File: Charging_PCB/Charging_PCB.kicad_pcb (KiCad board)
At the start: 2 copper layers, 89 x 59.5 mm, 15 parts, among them K3 BMS_Relay, K4 IMD_Relay, Q1 PMOS, Q2 PMOS, U112 Charger Input, U113 Signal Inputs, U114 Relay Output

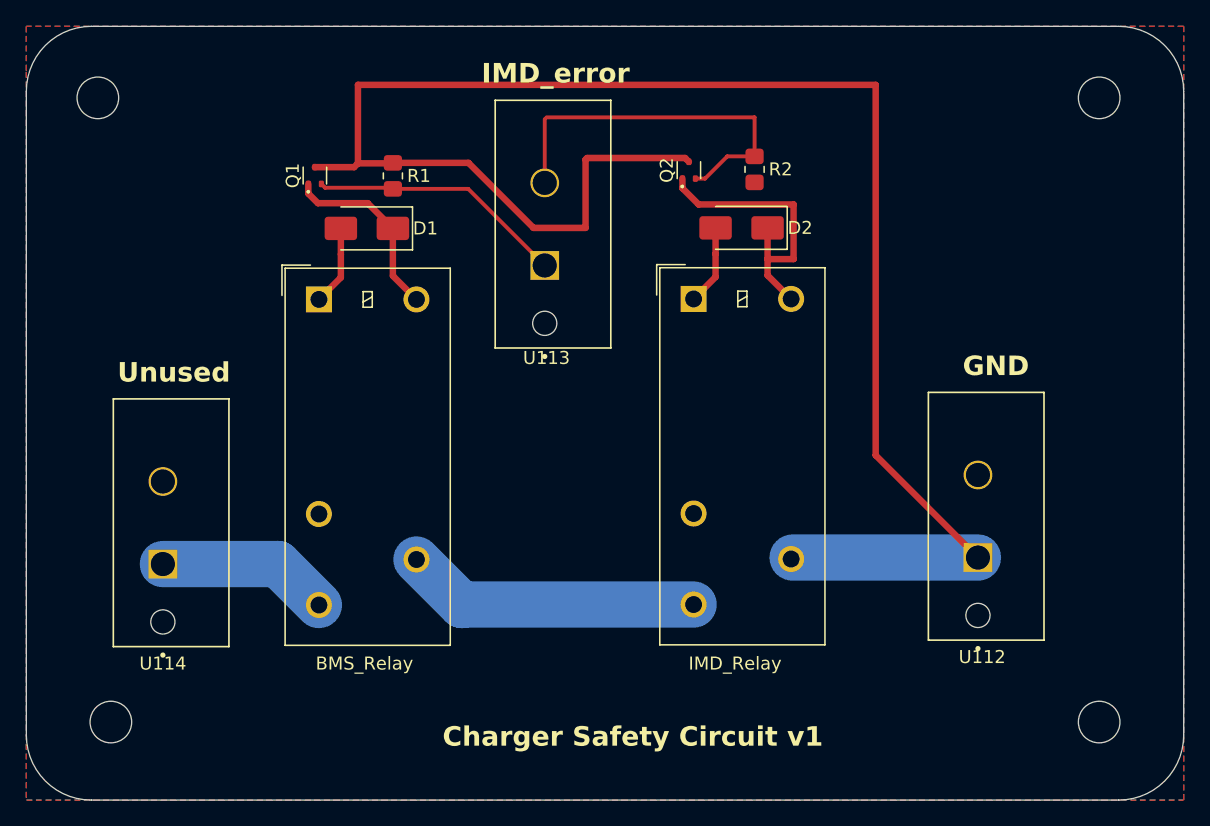
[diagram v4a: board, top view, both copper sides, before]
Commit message: Compacted PCB, and finished BOM,CPL,Gerbers(Charging)
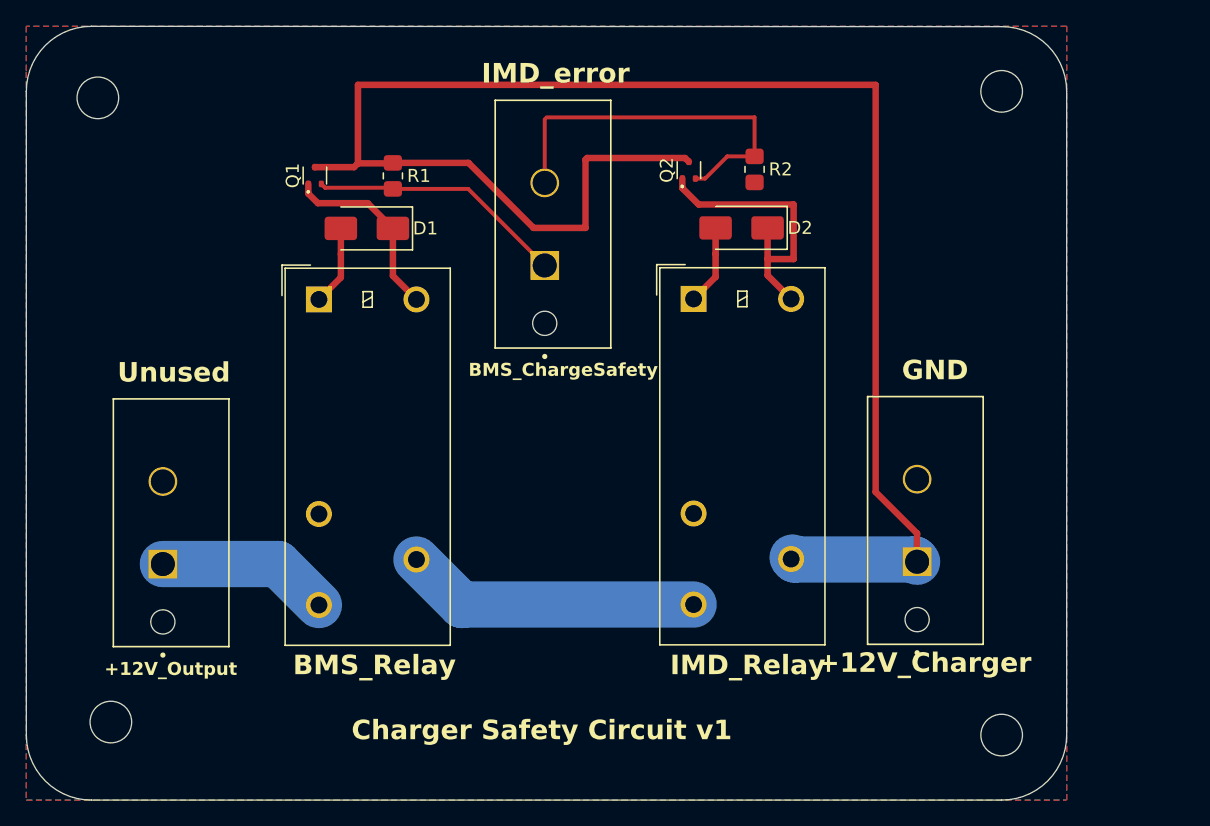
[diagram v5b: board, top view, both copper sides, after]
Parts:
- K3: value BMS_Relay -> Relay_SPDT_Omron_G2RL-1
- K4: value IMD_Relay -> Relay_SPDT_Omron_G2RL-1
- U112: value Charger Input -> 641964-1
- U113: value Signal Inputs -> 641964-1
- U114: value Relay Output -> 641964-1
- moved H103 7.57 mm to (181.5, 128.5)
- moved H101 7.52 mm to (181.5, 79.0)
- moved U112 4.69 mm to (175.0, 115.2)
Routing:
- net +12V: track 136.3 -> 130.1 mm
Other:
- board size 89 x 59.5 mm -> 80 x 59.5 mm
- board text added: "+12V_Charger"
- board text added: "+12V_Output"
- board text added: "BMS_ChargeSafety"
- board text added: "BMS_Relay"
- board text added: "IMD_Relay"

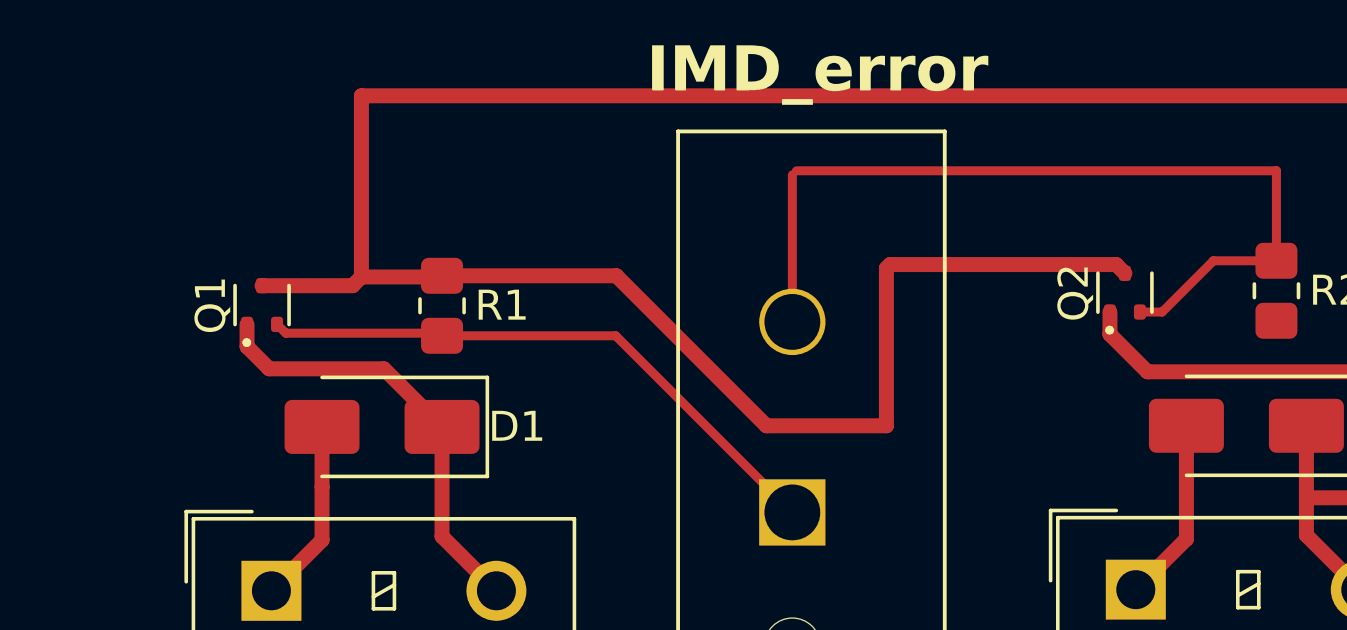
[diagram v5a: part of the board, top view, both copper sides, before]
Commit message: Fixed bad PMOS footprint and symbol, fixed gerbers/BOM/CPL
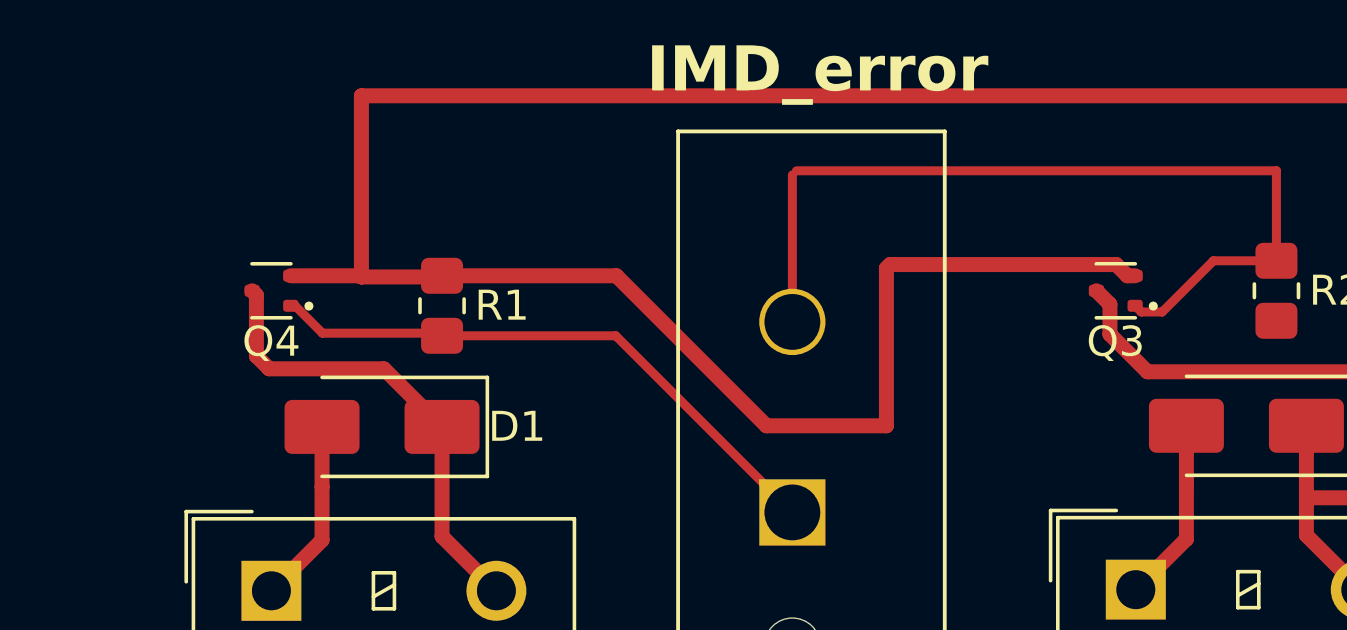
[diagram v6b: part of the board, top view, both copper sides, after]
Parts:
- removed Q1, Q2: PMOS, Package_TO_SOT_SMD:SOT-523
- added Q3: Q_PMOS_GSD, Library:SOT-523_Custom(C96676), F.Cu at (157.1, 85.0)
- added Q4: Q_PMOS_GSD, Library:SOT-523_Custom(C96676), F.Cu at (129.0, 85.0)
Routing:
- net Net-(D1-K): track 14.6 -> 15.6 mm
- net Net-(D2-K): track 22.2 -> 23.1 mm
- net +12V: track 130.1 -> 129.4 mm

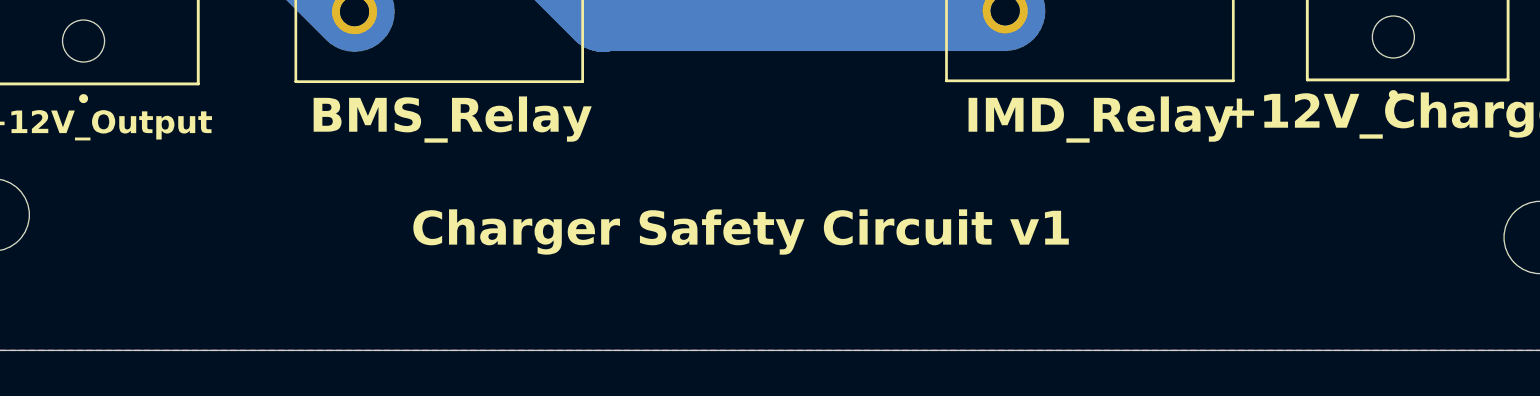
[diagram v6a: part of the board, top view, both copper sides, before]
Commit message: Fault latch added Logo
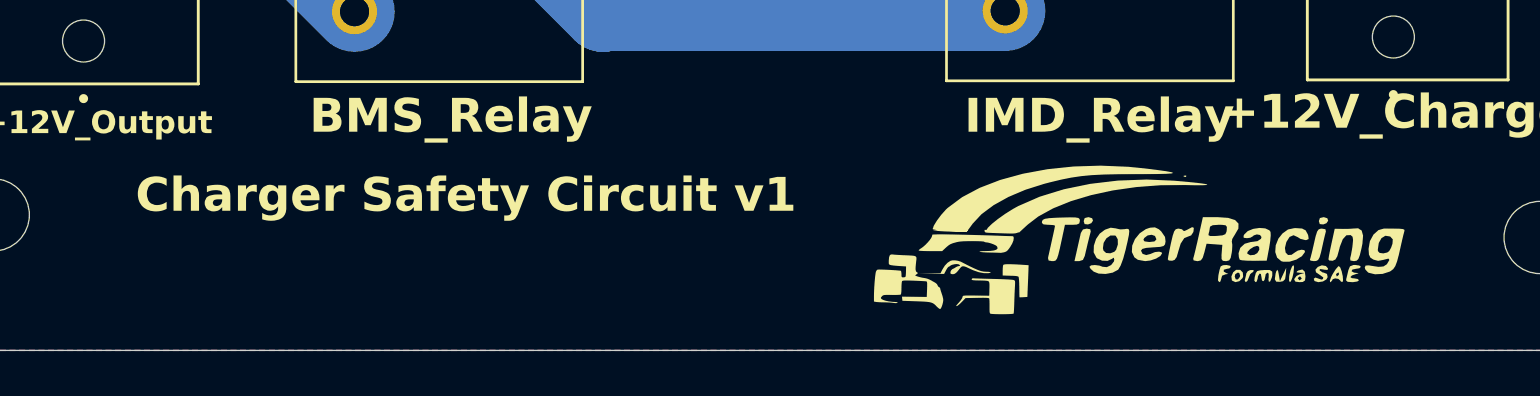
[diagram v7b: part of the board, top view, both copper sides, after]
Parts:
- added G***: LOGO, LOGO, F.Cu at (155.5, 130.1)
- added G***: LOGO, LOGO, F.Cu at (163.7, 128.7)

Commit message: CHARGE READY
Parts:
- added G***: LOGO, LOGO, F.Cu at (117.0, 94.5)
- moved U103 12.9 mm to (129.8, 114.2)
- moved K101 9.37 mm to (138.3, 94.0)
- moved U101 8.82 mm to (151.4, 85.1), turned to 180 degrees
- moved U102 8.25 mm to (166.8, 114.1)
- moved K102 5.78 mm to (152.1, 93.9)
- moved D102 4.61 mm to (165.0, 86.5)
- moved Q102 4.61 mm to (160.6, 82.0)
- moved R102 4.61 mm to (166.0, 82.0)
- moved D101 3.04 mm to (132.5, 86.5)
- moved Q101 3.04 mm to (128.8, 82.0)
- moved R101 3.04 mm to (134.5, 82.5)
- moved H104 2.24 mm to (112.0, 129.5)
- moved H102 1.12 mm to (182.0, 129.5)
- moved H101 0.71 mm to (182.0, 79.5)
- renumbered D1 to D101, D2 to D102, H103 to H102, H102 to H103, K3 to K101, K4 to K102, Q4 to Q101, Q3 to Q102, R1 to R101, R2 to R102, U113 to U101, U112 to U102, U114 to U103
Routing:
- net +12V: track 129.4 -> 88.2 mm
- net Net-(K101-Pad11): track 22.8 -> 7.75 mm
- net GND: track 12.3 -> 0.00 mm, vias 0 -> 295
- net /BMS_CSO: track 19.6 -> 29.5 mm
- net Net-(D101-K): track 15.6 -> 23.8 mm
- net /IMD_Error: track 29.6 -> 33.7 mm
- net /+12_Relay: track 13.3 -> 9.87 mm
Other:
- board size 80 x 59.5 mm -> 80 x 60 mm
